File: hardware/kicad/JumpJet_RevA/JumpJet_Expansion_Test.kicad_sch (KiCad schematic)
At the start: 17 parts, among them J10 QWIIC JST-SH, J11 EXPANSION

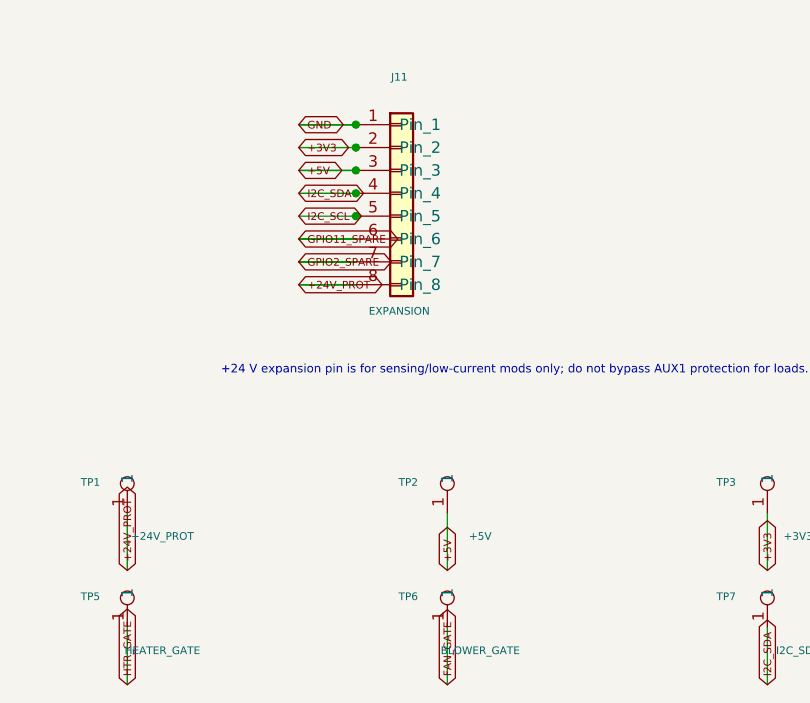
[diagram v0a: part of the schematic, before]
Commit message: hardware: separate gate power and default-disable heater driver
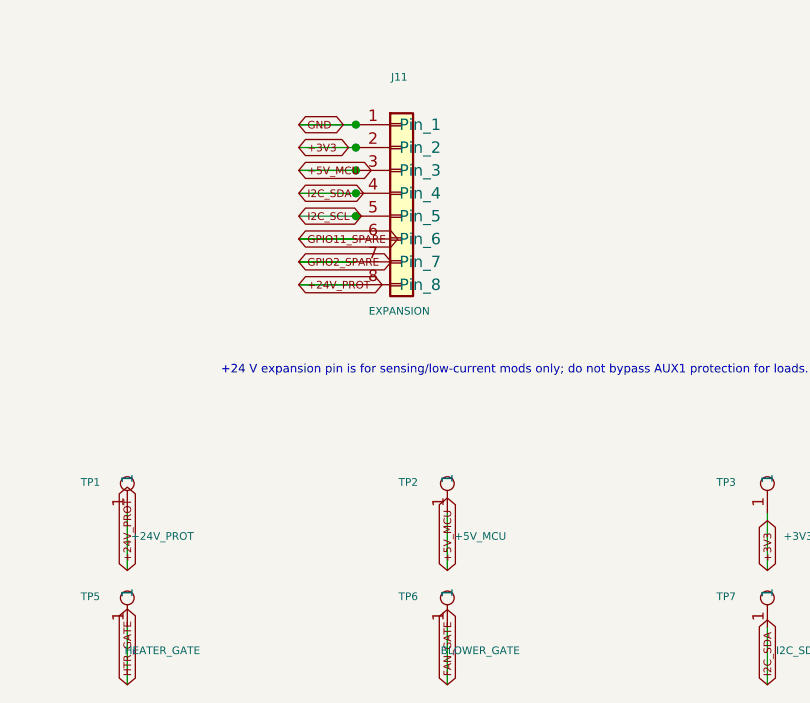
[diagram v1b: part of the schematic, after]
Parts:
- TP2: value +5V -> +5V_MCU
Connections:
- net +5V renamed +5V_MCU
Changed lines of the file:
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@@
     (effects (font (size 0.85 0.85)) (justify left bottom))
   )
-  (global_label "+5V" (shape bidirectional) (at 73.66 123.19 0) (fields_autoplaced)
-    (effects (font (size 0.85 0.85)) (justify left bottom))
-  )
-  (global_label "+5V" (shape bidirectional) (at 90.17 167.64 90) (fields_autoplaced)
+  (global_label "+5V_MCU" (shape bidirectional) (at 73.66 123.19 0) (fields_autoplaced)
+    (effects (font (size 0.85 0.85)) (justify left bottom))
+  )
+  (global_label "+5V_MCU" (shape bidirectional) (at 90.17 167.64 90) (fields_autoplaced)
     (effects (font (size 0.85 0.85)) (justify left bottom))
   )
@@
       (effects (font (size 0.85 0.85)))
     )
-    (property "Value" "+5V" (at 93.83 163.84 0)
-      (effects (font (size 0.85 0.85)))
-    )
+    (property "Value" "+5V_MCU" (at 93.83 163.84 0)
+      (effects (font (size 0.85 0.85)))
+    )
